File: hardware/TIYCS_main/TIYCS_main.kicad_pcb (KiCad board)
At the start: 2 copper layers, 100 x 100 mm, 50 parts, among them J1 USB4105-GF-A, J2 12vPWM, J3 WS2812B, J4 UART, J5 ExtSensor, J6 Terminal, J7 Barrel_Jack_Switch, J8 pinHeaders, Q1 NCE4060K, Q2 NCE4060K, Q3 2N7002, Q4 NCE4060K, Q5 NCE4060K, SW1 SW_Push, SW2 SW_Push, U1 ESP32-WROOM-32U, U2 CH340N, U3 MCP1703A-3302_SOT23

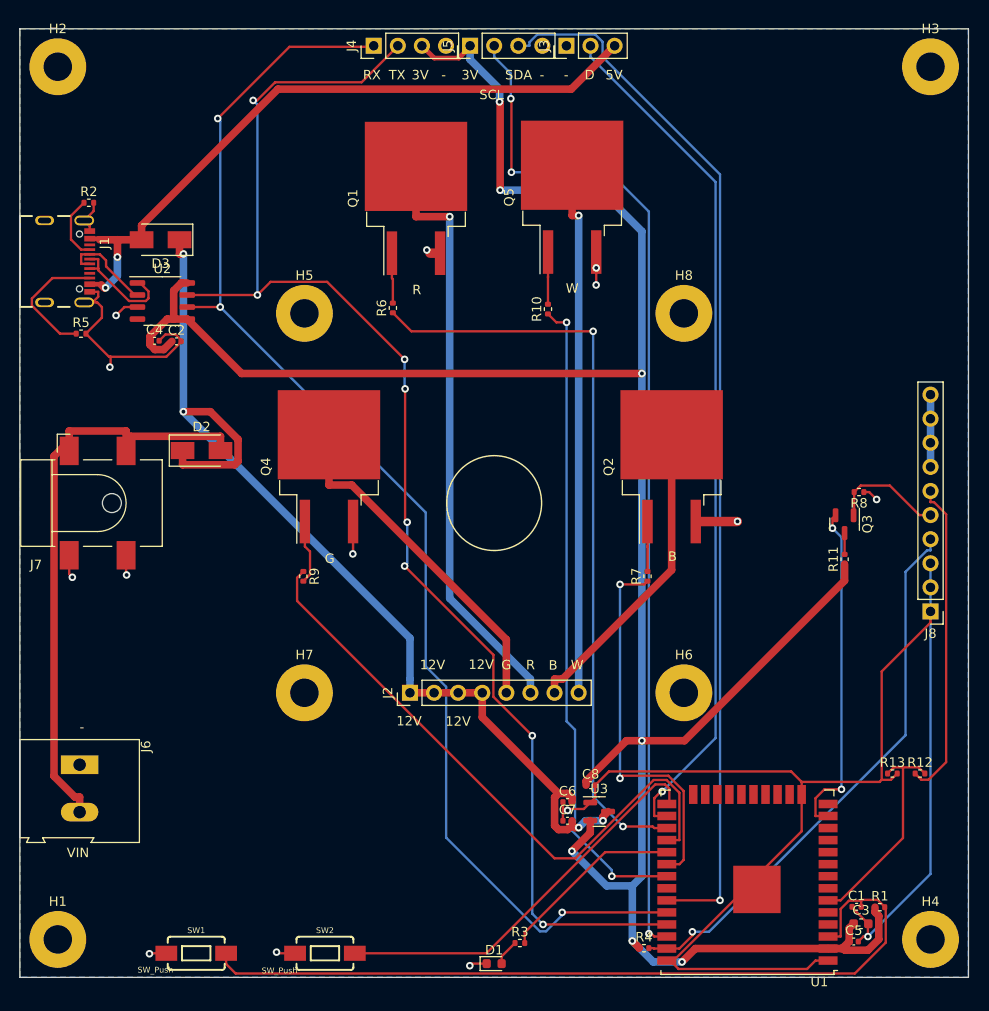
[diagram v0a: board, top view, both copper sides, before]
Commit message: Start with new LDO, fuse
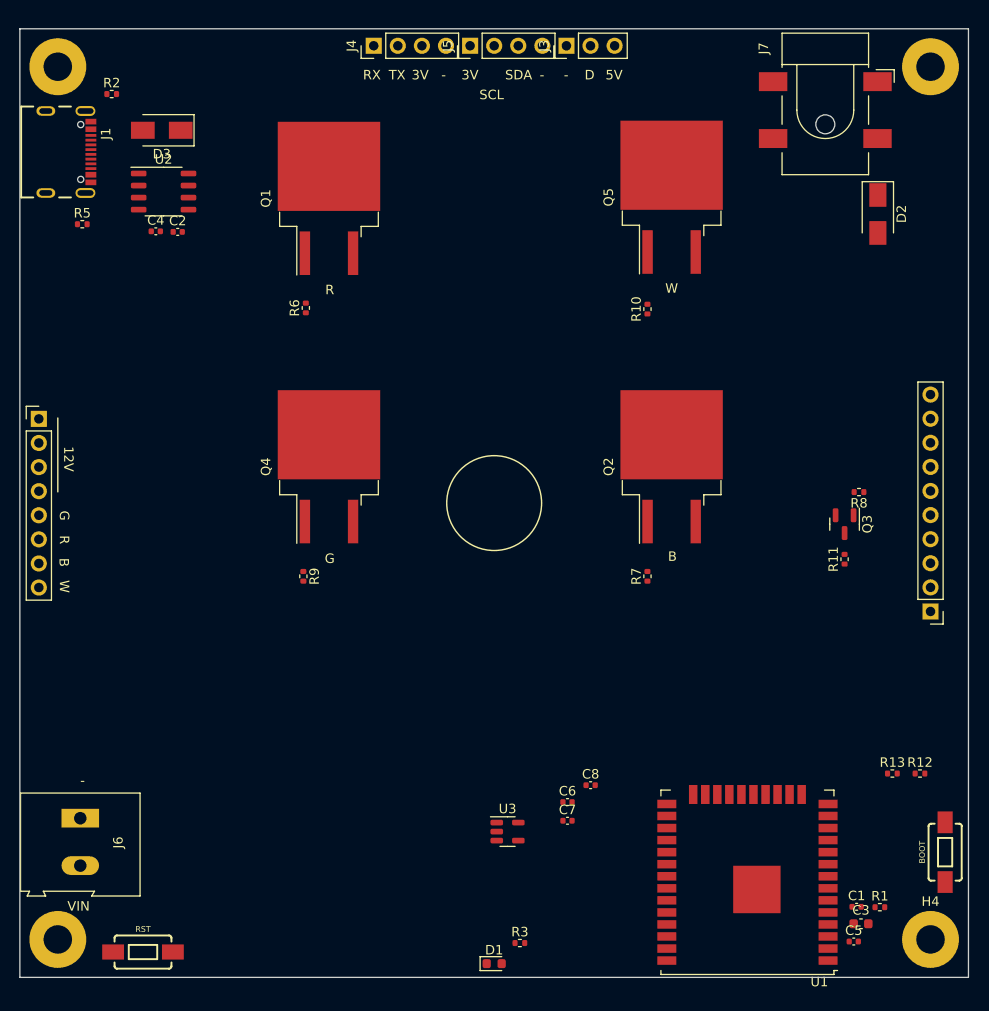
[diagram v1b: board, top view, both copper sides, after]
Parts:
- removed H5, H6, H7, H8: MountingHole, MountingHole:MountingHole_3mm_Pad
- removed R4: 100K, Resistor_SMD:R_0402_1005Metric
- BOOT: renamed from SW2; value SW_Push -> BOOT
- RST: renamed from SW1; value SW_Push -> RST
- U3: value MCP1703A-3302_SOT23 -> SPX3819M5-L-3-3; footprint Package_TO_SOT_SMD:SOT-23 -> Package_TO_SOT_SMD:SOT-23-5
- moved J7 87.2 mm to (84.9, 8.57), turned to -90 degrees
- moved D2 75.5 mm to (90.5, 19.5), turned to -90 degrees
- moved BOOT 66.2 mm to (97.5, 86.8), turned to 90 degrees
- moved J2 48.6 mm to (2.00, 41.1), turned to 0 degrees
- moved R2 11.7 mm to (9.68, 6.88)
- moved C2 11.5 mm to (16.6, 21.4)
- moved C4 11.5 mm to (14.3, 21.4)
- moved D3 11.5 mm to (15.0, 10.7)
- moved J1 11.5 mm to (2.73, 13.0)
- moved R5 11.5 mm to (6.58, 20.6)
- moved U2 11.5 mm to (15.2, 17.2)
- moved Q5 10.5 mm to (68.7, 17.8)
- moved R10 10.5 mm to (66.2, 29.6)
- moved U3 9.89 mm to (51.4, 84.6)
- moved R6 9.18 mm to (30.1, 29.4)
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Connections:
- C6 pad 2: 12V -> +12V
- C7 pad 2: 12V -> +12V
- D2 pad 1: 12V -> +12V
- D3 pad 1: 12V -> +12V
- J2 pad 1: 12V -> +12V
- J2 pad 2: 12V -> +12V
- J2 pad 3: 12V -> +12V
- J2 pad 4: 12V -> +12V
- J8 pad 4: EN -> GND
- U1 pad 37: EN -> unconnected-(U1-Pad37)
- U3 pad 1: GND -> +12V
- U3 pad 2: +3V3 -> GND
- U3 pad 3: 12V -> +12V
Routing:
- net +3V3: track 263.8 -> 0.00 mm, vias 7 -> 0
- net GND: track 210.1 -> 0.00 mm, vias 15 -> 0
- net TX: track 144.5 -> 0.00 mm, vias 8 -> 0
- net RX: track 137.1 -> 0.00 mm, vias 3 -> 0
- net SDA: track 111.2 -> 0.00 mm, vias 1 -> 0
- net 12V: track 109.5 -> 0.00 mm, vias 4 -> 0
- net SCL: track 108.4 -> 0.00 mm, vias 3 -> 0
- net DATA: track 90.7 -> 0.00 mm, vias 1 -> 0
- net Net-(C1-Pad2): track 86.5 -> 0.00 mm
- net R_PWM: track 80.1 -> 0.00 mm, vias 2 -> 0
- net VUSB: track 72.2 -> 0.00 mm, vias 2 -> 0
- net W_PWM: track 68.8 -> 0.00 mm, vias 2 -> 0
- net G_PWM: track 65.2 -> 0.00 mm
- net Net-(D2-Pad2): track 63.1 -> 0.00 mm
- net R: track 62.6 -> 0.00 mm, vias 1 -> 0
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- removed copper zone on B.Cu, net GND

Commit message: First version of ledPanel: board outline + pins
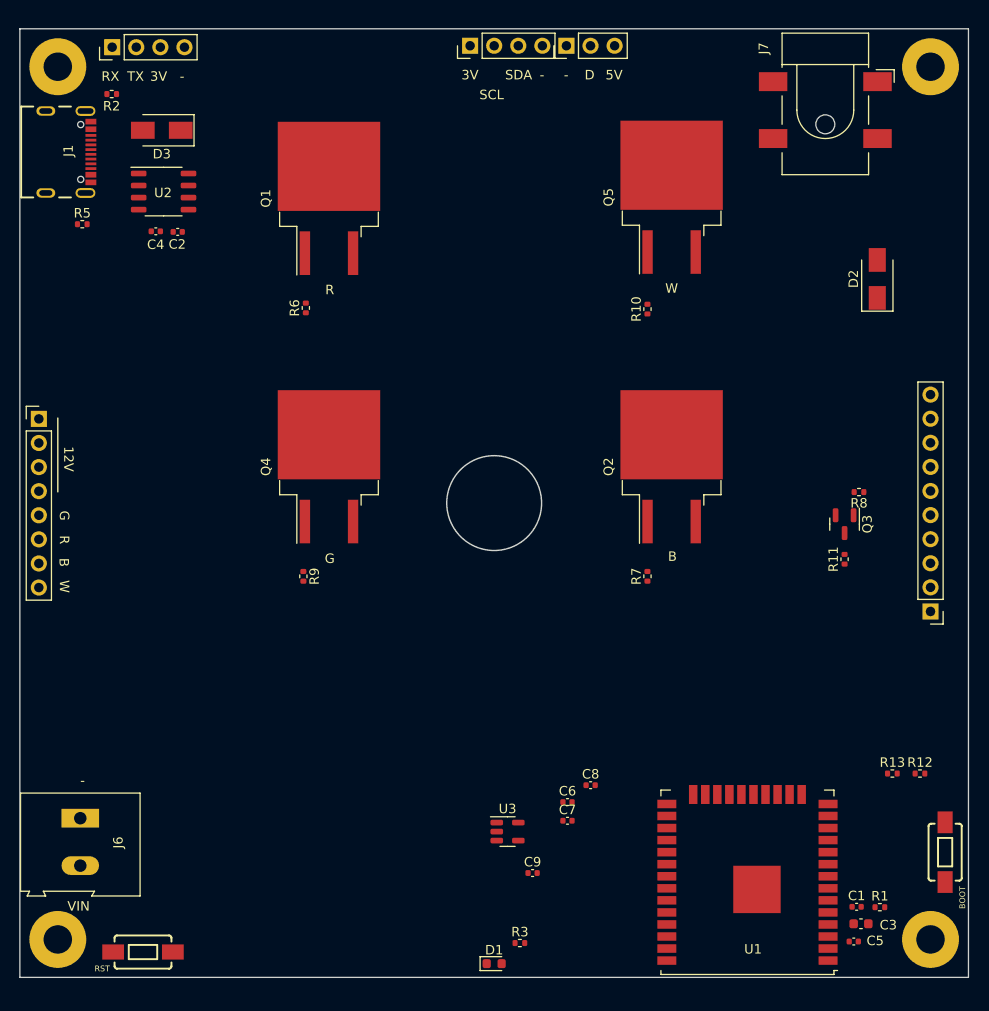
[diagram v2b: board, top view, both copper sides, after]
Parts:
- added C9: 10nF, Capacitor_SMD:C_0402_1005Metric, F.Cu at (54.0, 89.0)
- moved J4 27.6 mm to (9.73, 1.94)
- moved D2 6.85 mm to (90.4, 26.4), turned to 90 degrees
- renumbered RST to SW1, BOOT to SW2
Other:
- outline, holes or cut-outs redrawn
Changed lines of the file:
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@@
     (property "Sheetname" "")
     (attr exclude_from_pos_files)
-    (fp_text reference "H4" (at 0 -4) (layer "F.SilkS")
+    (fp_text reference "H4" (at 0 -4) (layer "F.SilkS") hide
       (effects (font (size 1 1) (thickness 0.15)))
     )
@@
     (property "Sheetname" "")
     (attr through_hole)
-    (fp_text reference "J3" (at 0 -2.33 90) (layer "F.SilkS")
+    (fp_text reference "J3" (at 0 -2.33 90) (layer "F.SilkS") hide
       (effects (font (size 1 1) (thickness 0.15)))
     )
@@
   )
   (footprint "Diode_SMD:D_SMA" (layer "F.Cu")
-    (at 90.45 19.52 -90)
+    (at 90.39 26.37 90)
     (descr "Diode SMA (DO-214AC)")
     (tags "Diode SMA (DO-214AC)")
@@
     (fp_line (start -0.64944 -0.79908) (end -0.64944 0.80112) (layer "F.Fab") (width 0.1))
     (fp_line (start 2.3 -1.5) (end -2.3 -1.5) (layer "F.Fab") (width 0.1))
-    (pad "1" smd rect locked (at -2 0 270) (size 2.5 1.8) (layers "F.Cu" "F.Paste" "F.Mask")
+    (pad "1" smd rect locked (at -2 0 90) (size 2.5 1.8) (layers "F.Cu" "F.Paste" "F.Mask")
       (net 25 "+12V") (pinfunction "K") (pintype "passive"))
-    (pad "2" smd rect locked (at 2 0 270) (size 2.5 1.8) (layers "F.Cu" "F.Paste" "F.Mask")
+    (pad "2" smd rect locked (at 2 0 90) (size 2.5 1.8) (layers "F.Cu" "F.Paste" "F.Mask")
       (net 6 "Net-(D2-Pad2)") (pinfunction "A") (pintype "passive"))
     (model "${KICAD6_3DMODEL_DIR}/Diode_SMD.3dshapes/D_SMA.wrl"
@@
   )
   (footprint "Connector_PinHeader_2.54mm:PinHeader_1x04_P2.54mm_Vertical" (layer "F.Cu")
-    (at 37.3025 1.79 90)
+    (at 9.73 1.94 90)
     (descr "Through hole straight pin header, 1x04, 2.54mm pitch, single row")
     (tags "Through hole pin header THT 1x04 2.54mm single row")
@@
     (property "Sheetname" "")
     (attr through_hole)
-    (fp_text reference "J4" (at 0 -2.33 90) (layer "F.SilkS")
+    (fp_text reference "J4" (at 0 -2.33 90) (layer "F.SilkS") hide
       (effects (font (size 1 1) (thickness 0.15)))
     )
@@
     (property "Sheetname" "")
     (attr smd)
-    (fp_text reference "C2" (at 0 -1.16) (layer "F.SilkS")
+    (fp_text reference "C2" (at -0.05 1.31) (layer "F.SilkS")
       (effects (font (size 1 1) (thickness 0.15)))
     )
@@
     (property "Sheetname" "")
     (attr smd)
-    (fp_text reference "U1" (at -7.58 -10.5) (layer "F.SilkS")
+    (fp_text reference "U1" (at -0.59 -7.055) (layer "F.SilkS")
       (effects (font (size 1 1) (thickness 0.15)))
     )
@@
     (property "Sheetname" "")
     (attr through_hole)
-    (fp_text reference "J1" (at -1.925 -6.335 90) (layer "F.SilkS")
+    (fp_text reference "J1" (at -0.1275 -2.385 90) (layer "F.SilkS")
       (effects (font (size 1 1) (thickness 0.015)))
     )
@@
     (property "Sheetname" "")
     (attr through_hole)
-    (fp_text reference "J5" (at 0 -2.33 90) (layer "F.SilkS")
+    (fp_text reference "J5" (at 0.02 -2.8325 90) (layer "F.SilkS") hide
       (effects (font (size 1 1) (thickness 0.15)))
     )
@@
     (property "Sheetname" "")
     (attr smd)
-    (fp_text reference "RST" (at 0 -2.413) (layer "F.SilkS")
+    (fp_text reference "SW1" (at 0 -2.413) (layer "F.SilkS") hide
       (effects (font (size 0.6096 0.6096) (thickness 0.127)))
     )
-    (fp_text value "RST" (at -4.3 1.75) (layer "F.SilkS") hide
+    (fp_text value "RST" (at -4.3 1.75) (layer "F.SilkS")
       (effects (font (size 0.6096 0.6096) (thickness 0.127)))
     )
@@
     (property "Sheetname" "")
     (attr smd)
-    (fp_text reference "C5" (at 0 -1.16) (layer "F.SilkS")
+    (fp_text reference "C5" (at 2.26 -0.08) (layer "F.SilkS")
       (effects (font (size 1 1) (thickness 0.15)))
     )
@@
     (property "Sheetname" "")
     (attr smd)
-    (fp_text reference "U2" (at 0 -3.4) (layer "F.SilkS")
+    (fp_text reference "U2" (at -0.06 0.13) (layer "F.SilkS")
       (effects (font (size 1 1) (thickness 0.15)))
     )
@@
     (property "Sheetname" "")
     (attr smd)
-    (fp_text reference "C4" (at 0 -1.16) (layer "F.SilkS")
+    (fp_text reference "C4" (at -0.01 1.4) (layer "F.SilkS")
       (effects (font (size 1 1) (thickness 0.15)))
     )
@@
     (property "Sheetname" "")
     (attr smd)
-    (fp_text reference "BOOT" (at 0 -2.413 90) (layer "F.SilkS")
+    (fp_text reference "SW2" (at 0 -2.413 90) (layer "F.SilkS") hide
       (effects (font (size 0.6096 0.6096) (thickness 0.127)))
     )
-    (fp_text value "BOOT" (at -4.79 1.83 90) (layer "F.SilkS") hide
+    (fp_text value "BOOT" (at -4.79 1.83 90) (layer "F.SilkS")
       (effects (font (size 0.6096 0.6096) (thickness 0.127)))
     )
@@
     (property "Sheetname" "")
     (attr smd)
-    (fp_text reference "C3" (at 0 -1.43) (layer "F.SilkS")
+    (fp_text reference "C3" (at 2.88 0.13) (layer "F.SilkS")
       (effects (font (size 1 1) (thickness 0.15)))
     )
@@
     )
   )
+  (footprint "Capacitor_SMD:C_0402_1005Metric" (layer "F.Cu")
+    (at 54.05 89)
+    (descr "Capacitor SMD 0402 (1005 Metric), square (rectangular) end terminal, IPC_7351 nominal, (Body size source: IPC-SM-782 page 76, https://www.pcb-3d.com/wordpress/wp-content/uploads/ipc-sm-782a_amendment_1_and_2.pdf), generated with kicad-footprint-generator")
+    (tags "capacitor")
+    (property "JLCPCB" " C15195 ")
+    (property "Sheetfile" "TIYCS_main.kicad_sch")
+    (property "Sheetname" "")
+    (attr smd)
+    (fp_text reference "C9" (at 0 -1.16) (layer "F.SilkS")
+      (effects (font (size 1 1) (thickness 0.15)))
+    )
+    (fp_text value "10nF" (at 0 1.16) (layer "F.Fab")
+      (effects (font (size 1 1) (thickness 0.15)))
+    )
+    (fp_text user "${REFERENCE}" (at 0 0) (layer "F.Fab")
+      (effects (font (size 0.25 0.25) (thickness 0.04)))
+    )
+    (fp_line (start -0.107836 -0.36) (end 0.107836 -0.36) (layer "F.SilkS") (width 0.12))
+    (fp_line (start -0.107836 0.36) (end 0.107836 0.36) (layer "F.SilkS") (width 0.12))
+    (fp_line (start 0.91 -0.46) (end 0.91 0.46) (layer "F.CrtYd") (width 0.05))
+    (fp_line (start -0.91 -0.46) (end 0.91 -0.46) (layer "F.CrtYd") (width 0.05))
+    (fp_line (start -0.91 0.46) (end -0.91 -0.46) (layer "F.CrtYd") (width 0.05))
+    (fp_line (start 0.91 0.46) (end -0.91 0.46) (layer "F.CrtYd") (width 0.05))
+    (fp_line (start -0.5 0.25) (end -0.5 -0.25) (layer "F.Fab") (width 0.1))
+    (fp_line (start 0.5 -0.25) (end 0.5 0.25) (layer "F.Fab") (width 0.1))
+    (fp_line (start 0.5 0.25) (end -0.5 0.25) (layer "F.Fab") (width 0.1))
+    (fp_line (start -0.5 -0.25) (end 0.5 -0.25) (layer "F.Fab") (width 0.1))
+    (pad "1" smd roundrect locked (at -0.48 0) (size 0.56 0.62) (layers "F.Cu" "F.Paste" "F.Mask") (roundrect_rratio 0.25)
+      (net 23 "Net-(C9-Pad1)") (pintype "passive"))
+    (pad "2" smd roundrect locked (at 0.48 0) (size 0.56 0.62) (layers "F.Cu" "F.Paste" "F.Mask") (roundrect_rratio 0.25)
+      (net 1 "GND") (pintype "passive"))
+    (model "${KICAD6_3DMODEL_DIR}/Capacitor_SMD.3dshapes/C_0402_1005Metric.wrl"
+      (offset (xyz 0 0 0))
+      (scale (xyz 1 1 1))
+      (rotate (xyz 0 0 0))
+    )
+  )
   (footprint "Resistor_SMD:R_0402_1005Metric" (layer "F.Cu")
     (at 86.94 55.92 90)
@@
     (property "Sheetname" "")
     (attr smd)
-    (fp_text reference "R2" (at 0 -1.17) (layer "F.SilkS")
+    (fp_text reference "R2" (at -0.01 1.27) (layer "F.SilkS")
       (effects (font (size 1 1) (thickness 0.15)))
     )
@@
   )
   (gr_line (start 4 48.82) (end 4 41.03) (layer "F.SilkS") (width 0.15))
-  (gr_circle (center 50 50) (end 55 50) (layer "F.SilkS") (width 0.15) (fill none))
   (gr_rect locked (start 0 0) (end 100 100) (layer "Edge.Cuts") (width 0.1) (fill none))
+  (gr_circle (center 50 50) (end 55 50) (layer "Edge.Cuts") (width 0.15) (fill none))
   (gr_text "-" (at 57.59 4.87) (layer "F.SilkS")
     (effects (font (size 1 1) (thickness 0.25)))
   )
-  (gr_text "3V" (at 42.2 4.87) (layer "F.SilkS")
+  (gr_text "3V" (at 14.6275 5.02) (layer "F.SilkS")
     (effects (font (size 1 1) (thickness 0.25)))
   )
@@
     (effects (font (size 1 1) (thickness 0.25)))
   )
-  (gr_text "TX" (at 39.77 4.87) (layer "F.SilkS")
-    (effects (font (size 1 1) (thickness 0.25)))
-  )
-  (gr_text "-" (at 44.67 4.87) (layer "F.SilkS")
+  (gr_text "TX" (at 12.1975 5.02) (layer "F.SilkS")
+    (effects (font (size 1 1) (thickness 0.25)))
+  )
+  (gr_text "-" (at 17.0975 5.02) (layer "F.SilkS")
     (effects (font (size 1 1) (thickness 0.25)))
   )
@@
     (effects (font (size 1 1) (thickness 0.25)))
   )
-  (gr_text "RX" (at 37.11 4.87) (layer "F.SilkS")
+  (gr_text "RX" (at 9.5375 5.02) (layer "F.SilkS")
     (effects (font (size 1 1) (thickness 0.25)))
   )
@@
     (effects (font (size 1 1) (thickness 0.25)))
   )
-  (group "" (id 00e6af4a-188f-44ff-b206-a29b90405e95)
-    (members
-      252e1042-e48a-498a-b5f2-09c3a6577ad4
-      2ce9cfb9-d68a-4e79-a585-967f4babe781
-      837c91ba-c66a-4000-849e-3e16a4f593d0
-    )
-  )
   (group "" (id 12f83182-9ff2-4e0f-86cb-6304e859169e)

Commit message: Connector on motherboard aligned with ledPanel
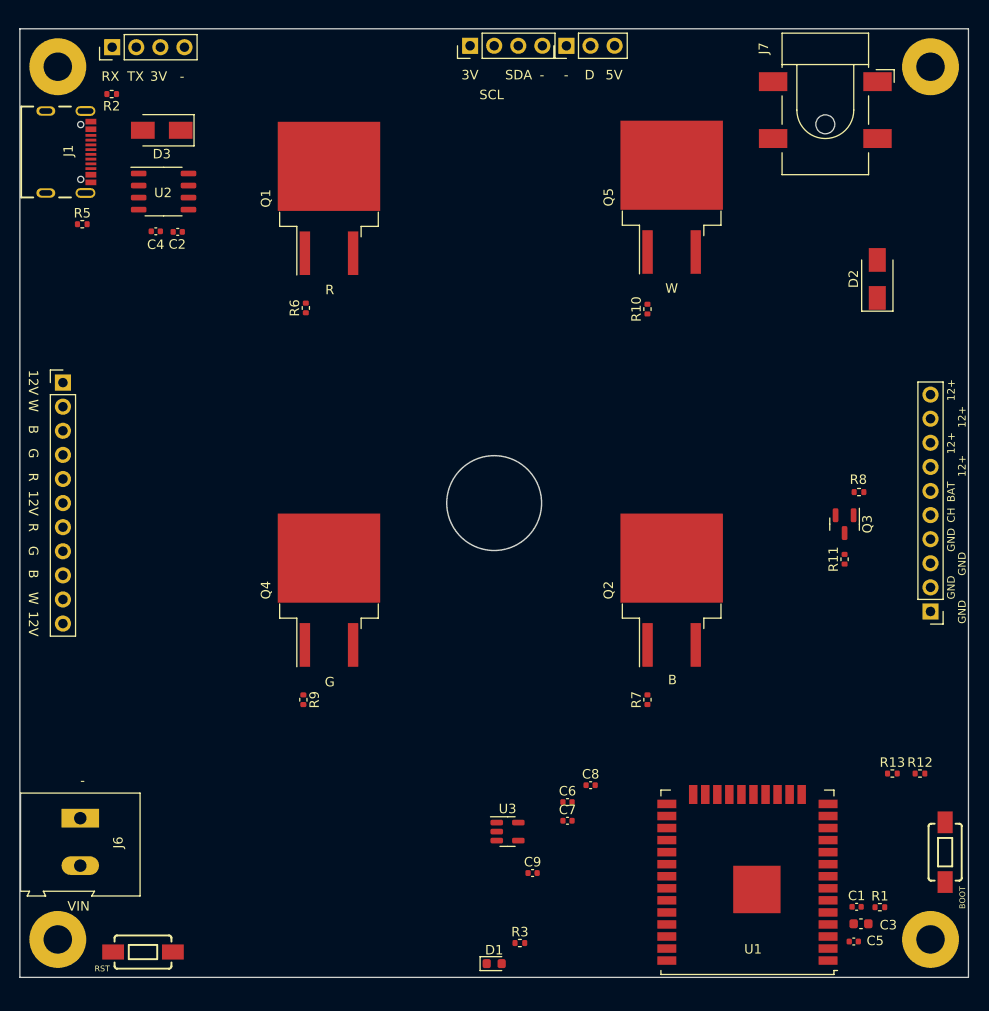
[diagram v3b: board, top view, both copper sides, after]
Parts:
- J2: footprint Connector_PinHeader_2.54mm:PinHeader_1x08_P2.54mm_Vertical -> Connector_PinHeader_2.54mm:PinHeader_1x11_P2.54mm_Vertical
- moved R7 13.0 mm to (66.2, 70.7)
- moved R9 13.0 mm to (29.9, 70.7)
- moved Q2 13.0 mm to (68.7, 59.2)
- moved Q4 13.0 mm to (32.6, 59.2)
- moved J2 4.59 mm to (4.54, 37.3)
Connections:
- J2 pad 2: +12V -> W
- J2 pad 3: +12V -> B
- J2 pad 4: +12V -> G
- J2 pad 5: G -> R
- J2 pad 6: R -> +12V
- J2 pad 7: B -> R
- J2 pad 8: W -> G
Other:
- board text added: "12+"
- board text added: "BAT"
- board text added: "CH"
- board text added: "GND"
